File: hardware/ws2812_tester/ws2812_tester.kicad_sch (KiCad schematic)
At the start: 12 parts, among them J1 USB_C_DEALON-USB-US31-106, J2 Pins_1-4, J3 Conn_01x03, J4 Pins_5-8, Q1 PMN48XP, U1 ATtiny85-20S

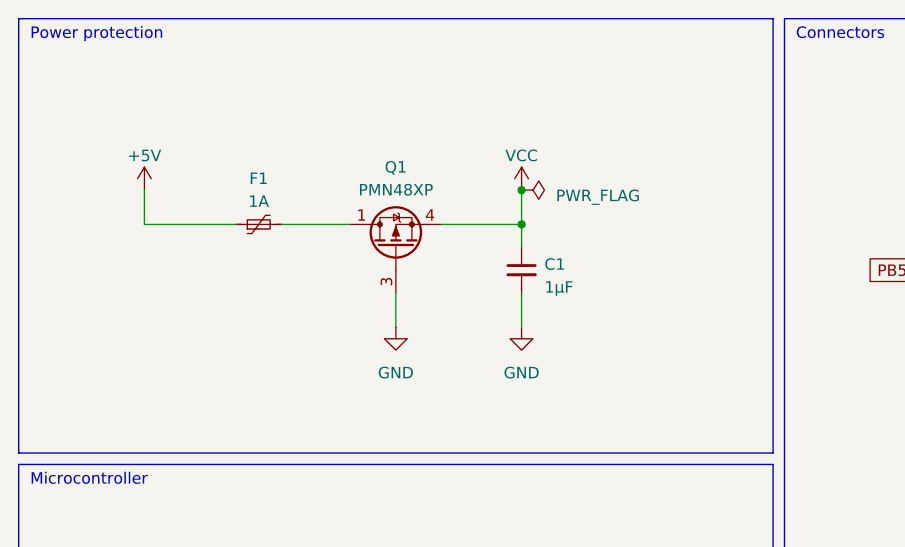
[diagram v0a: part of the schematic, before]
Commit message: Adds power indication LEDs
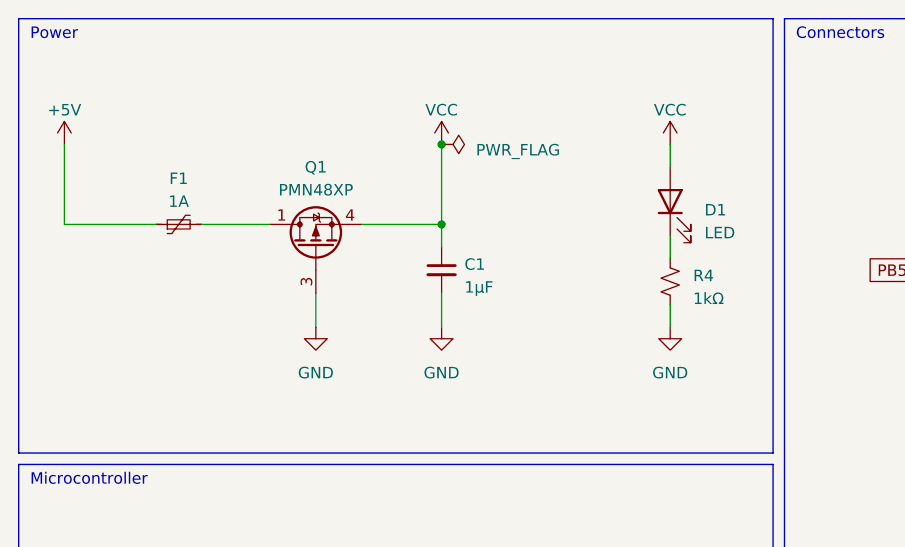
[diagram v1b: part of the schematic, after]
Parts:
- added D1: LED, symbol Device:LED
- added R4: 1kΩ, Resistor_SMD:R_0805_2012Metric_Pad1.20x1.40mm_HandSolder, symbol Device:R_Small_US
- C1, C2: footprint (none) -> Capacitor_SMD:C_0805_2012Metric_Pad1.18x1.45mm_HandSolder
- F1: footprint (none) -> ws2812_tester:Belfuse_0ZCJ
- J2, J4: footprint (none) -> Connector_PinHeader_2.54mm:PinHeader_1x04_P2.54mm_Vertical
- J3: footprint (none) -> Connector_PinHeader_2.54mm:PinHeader_1x03_P2.54mm_Horizontal
- R1, R2, R3: footprint (none) -> Resistor_SMD:R_0805_2012Metric_Pad1.20x1.40mm_HandSolder
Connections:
- net GND: now also R4.2
- net VCC: now also D1.2 (A)
- new net: D1.1 (K), R4.1
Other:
- note added: "Power"
- note removed: "Power protection"
- moved on the sheet: C1, F1, Q1

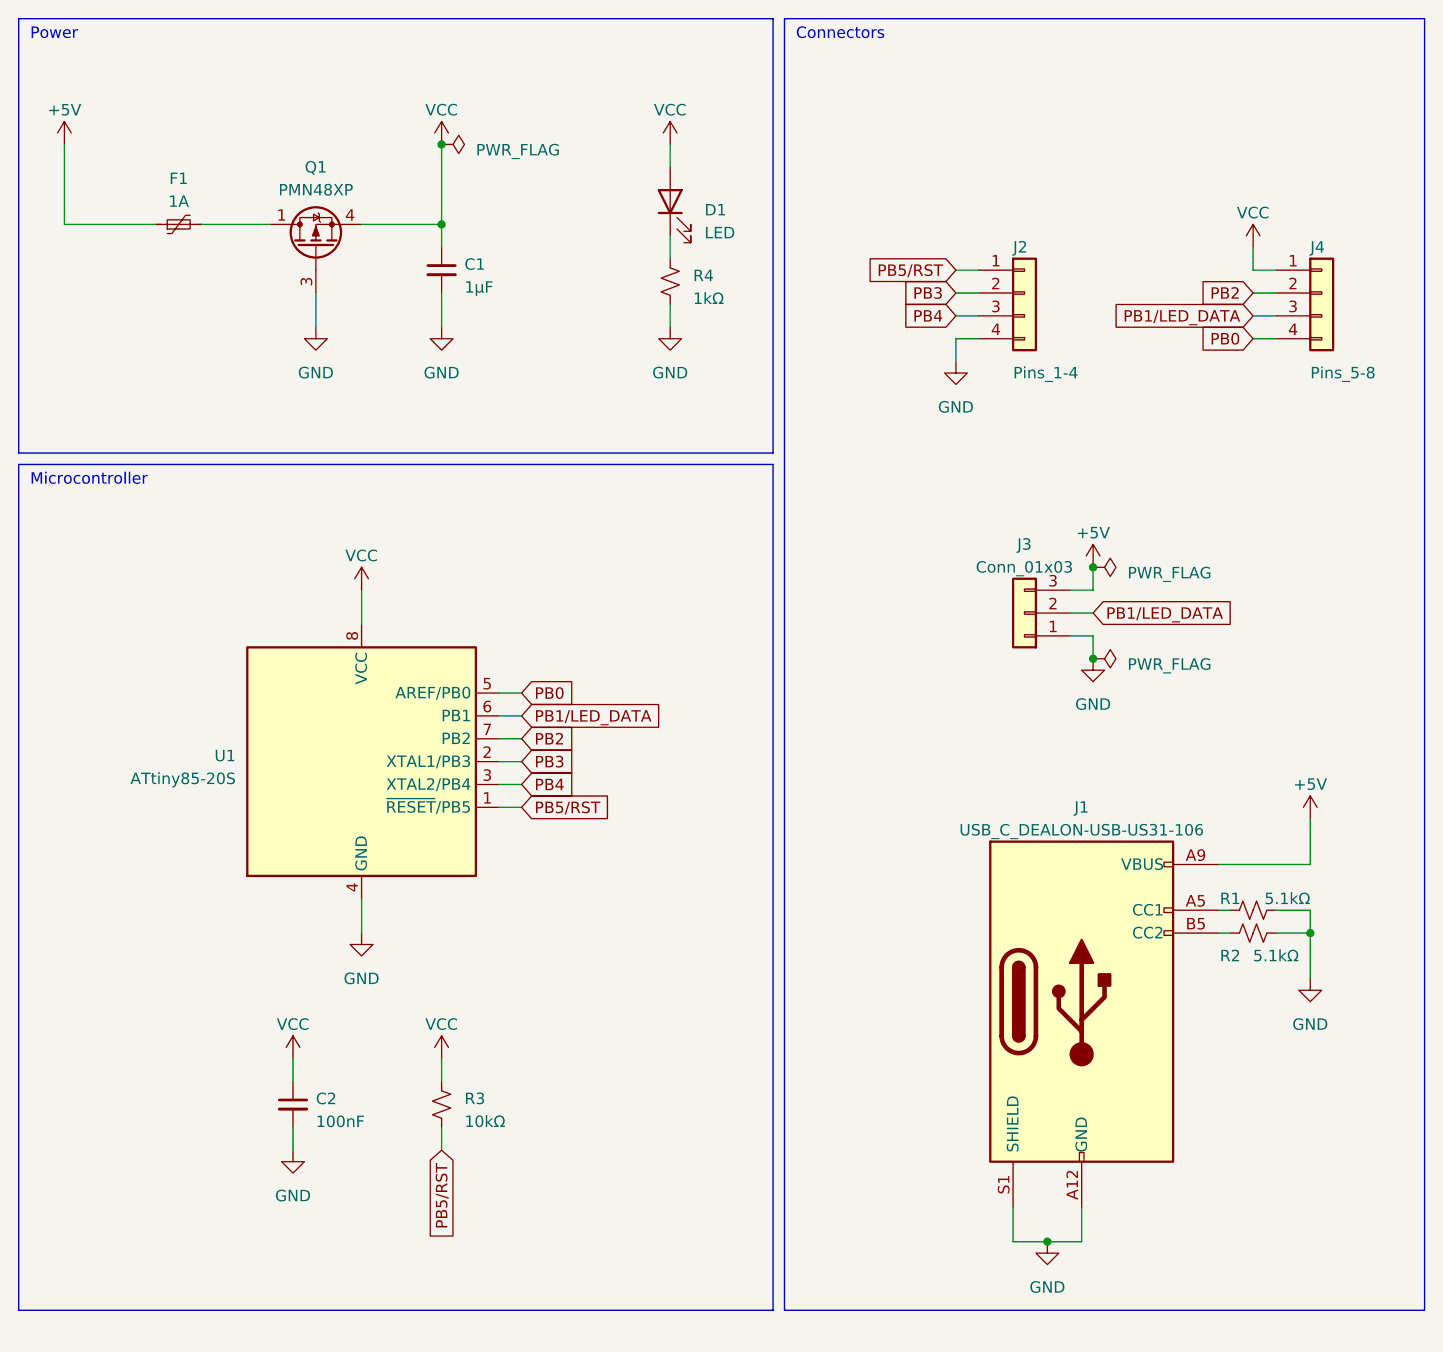
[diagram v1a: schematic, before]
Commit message: Changes schematic so the board is never powered by the LED strip
The idea is that since this is a tester, it will provide the power to
the LED strip. We add a schottky diode to protect the board just in case
it is connected to an already powered strip.

Since we'll always power the board from a usb-c connector, we don't need
reverse polarity protection anymore.
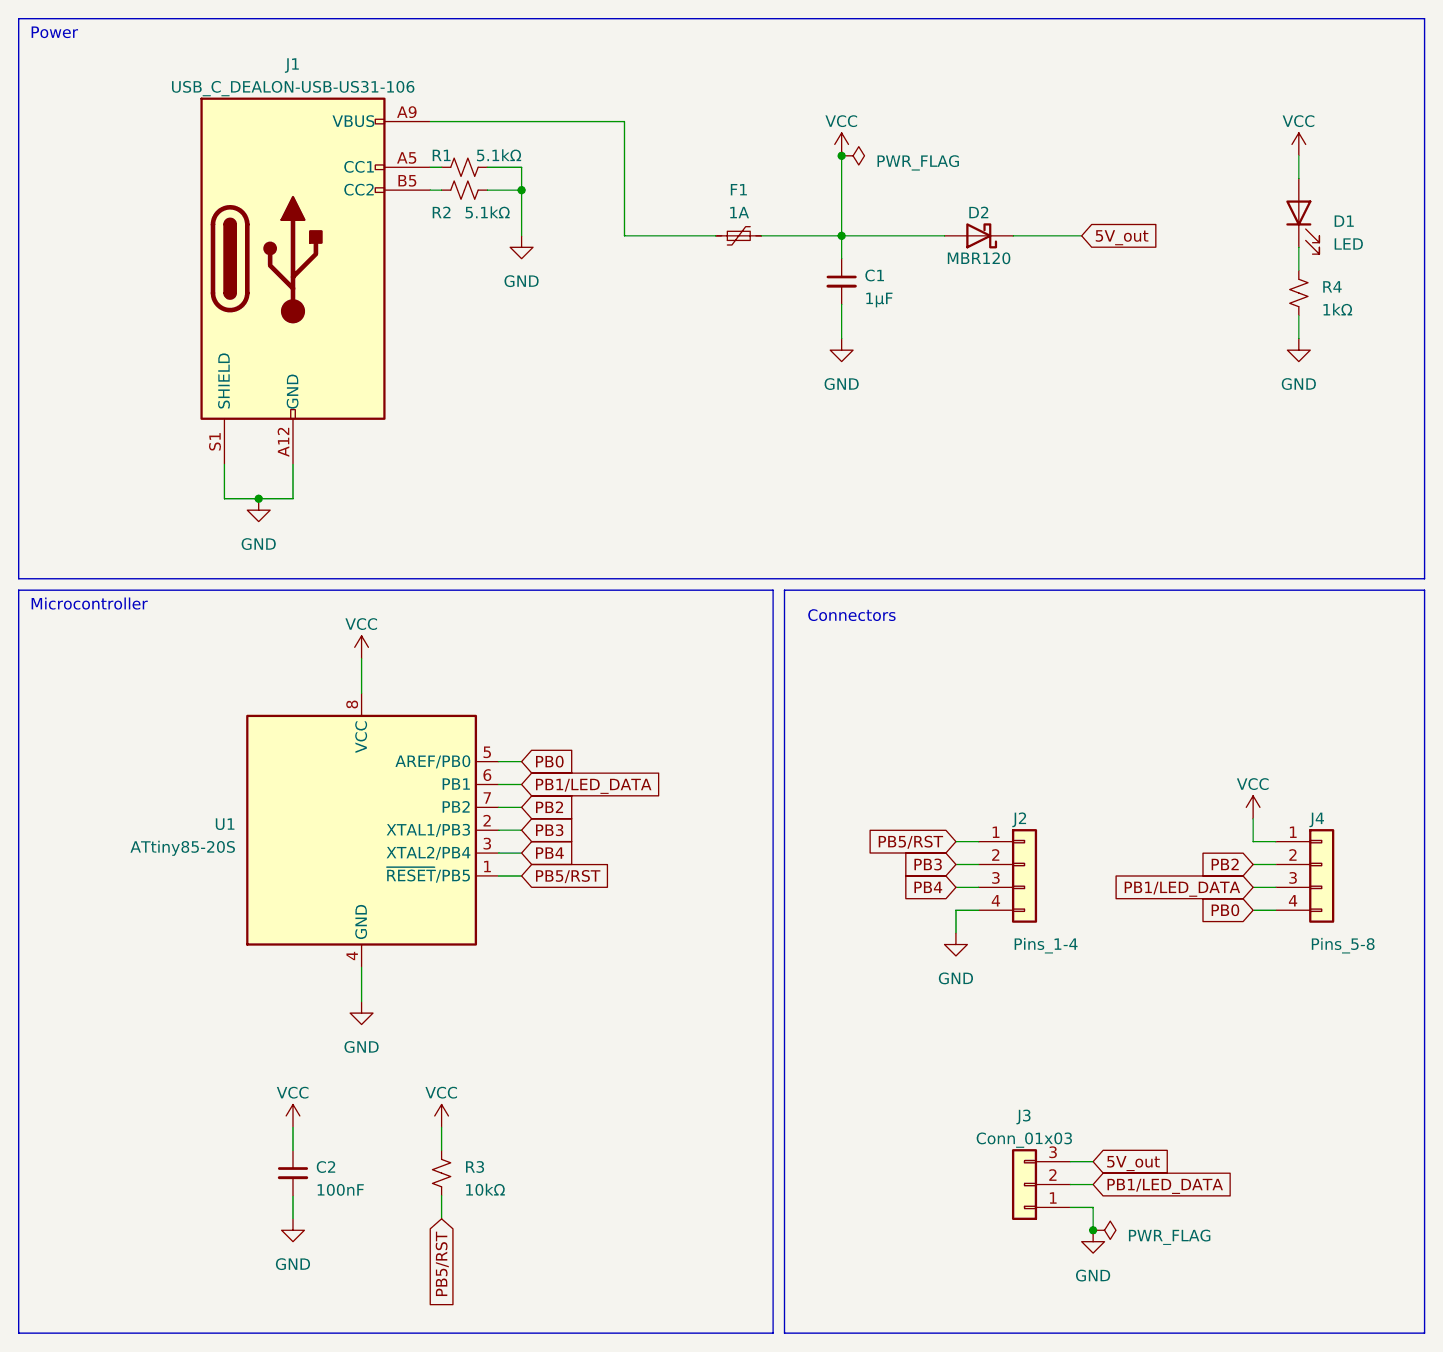
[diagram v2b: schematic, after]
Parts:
- removed Q1: PMN48XP, Package_SO:TSOP-6_1.65x3.05mm_P0.95mm, symbol Transistor_FET:PMN48XP
- added D2: MBR120, Diode_SMD:D_SOD-123, symbol Device:D_Schottky
- D1: footprint (none) -> LED_SMD:LED_0603_1608Metric_Pad1.05x0.95mm_HandSolder
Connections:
- net VCC: now also F1.2, D2.2 (A)
- net +5V: no longer names the net of F1.1, J1.A9 (VBUS), J1.B9 (VBUS)
- net +5V: no longer J3.3 (Pin_3)
- new net 5V_out: D2.1 (K), J3.3 (Pin_3)
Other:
- moved on the sheet: C1, C2, D1, F1, J1, J2, J3, J4, R1, R2, R3, R4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
